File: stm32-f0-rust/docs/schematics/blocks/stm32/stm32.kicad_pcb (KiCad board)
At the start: 2 copper layers, 3 parts, among them J1 Conn_01x05_Female, J2 Conn_01x02_Female, U1 STM32F042F4Px

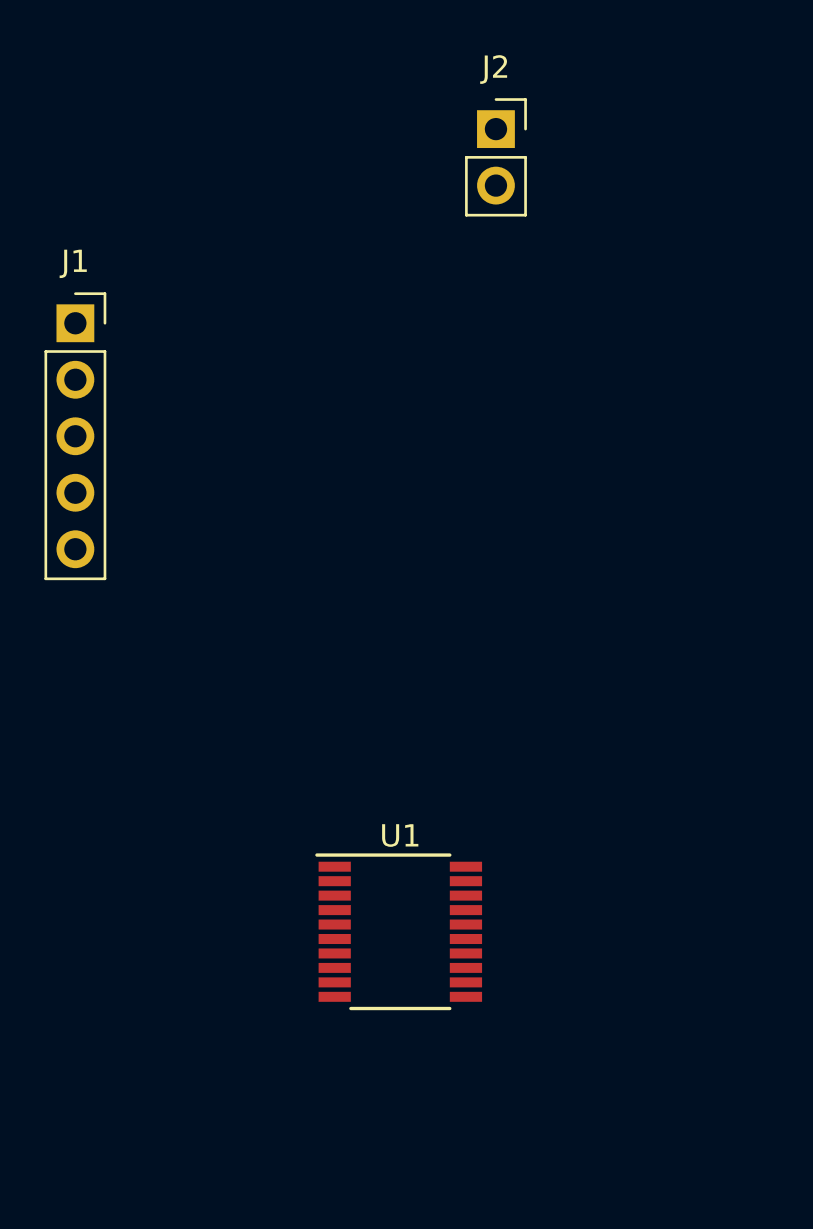
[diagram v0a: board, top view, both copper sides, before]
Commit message: [PCB][STM32-Block] Use single 7-pin socket instead of two.
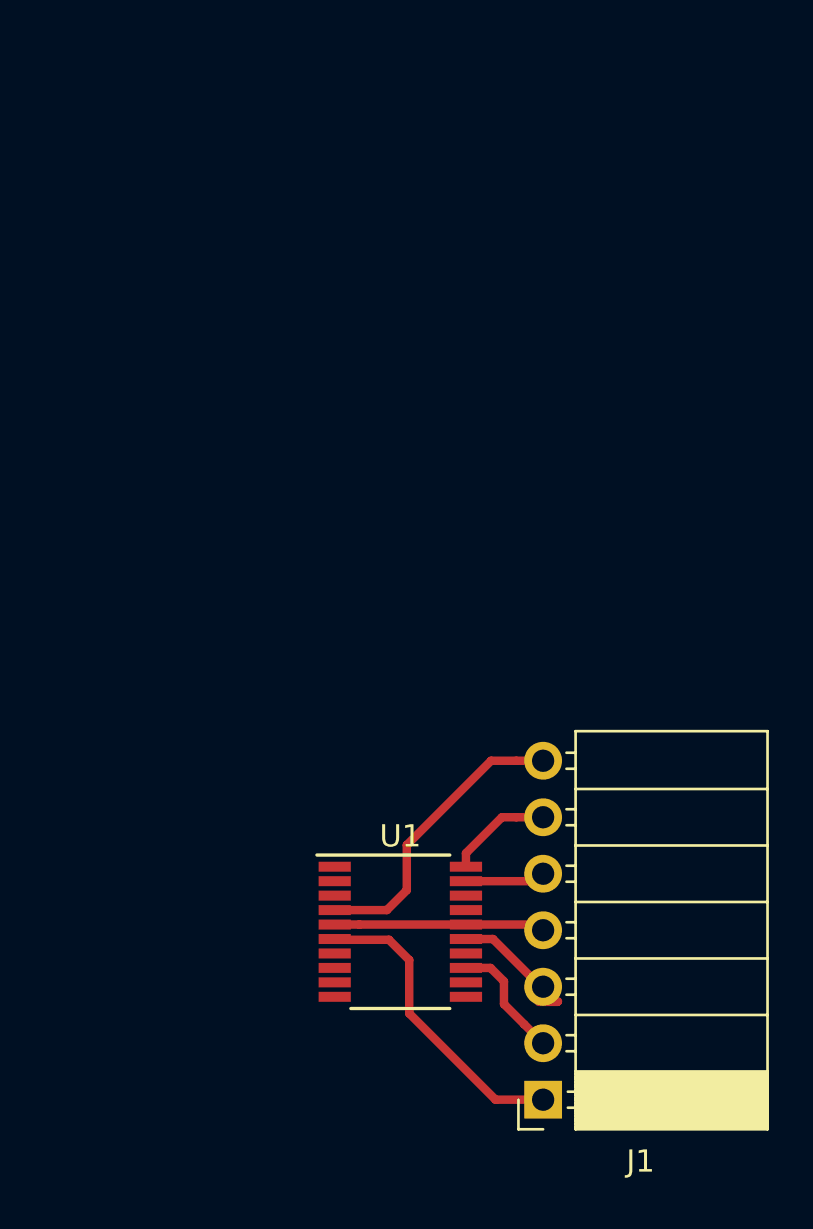
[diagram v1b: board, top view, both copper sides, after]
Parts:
- removed J2: Conn_01x02_Female, Connector_PinSocket_2.54mm:PinSocket_1x02_P2.54mm_Vertical
- J1: value Conn_01x05_Female -> Conn_01x07_Female; footprint Connector_PinSocket_2.54mm:PinSocket_1x05_P2.54mm_Vertical -> Connector_PinSocket_2.54mm:PinSocket_1x07_P2.54mm_Horizontal
- moved J1 40.8 mm to (164.4, 104.7), turned to 180 degrees
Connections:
- J1 pad 1: VDD -> Button
- J1 pad 2: SWCLK -> Buzzer
- J1 pad 4: SWDIO -> VDD
- J1 pad 5: NRST -> SWDIO
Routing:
- net Button: track 0.00 -> 13.8 mm
- net NRST: track 0.00 -> 13.3 mm
- net VDD: track 0.00 -> 9.48 mm
- net Buzzer: track 0.00 -> 5.47 mm
- net GND: track 0.00 -> 5.33 mm
- net SWCLK: track 0.00 -> 5.25 mm
- net SWDIO: track 0.00 -> 3.61 mm

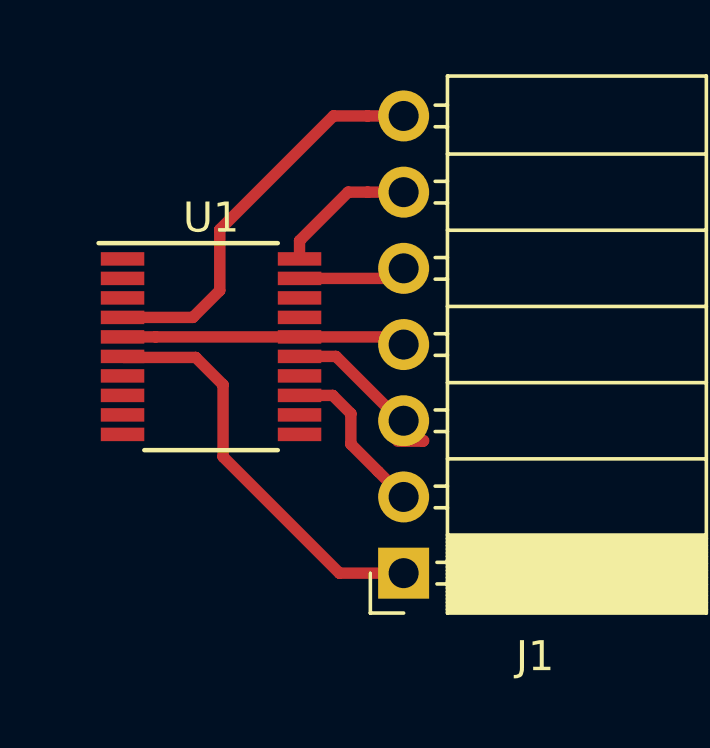
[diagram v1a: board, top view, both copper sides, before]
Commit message: [PCB][STM32-Block] Reduce PCB edges.
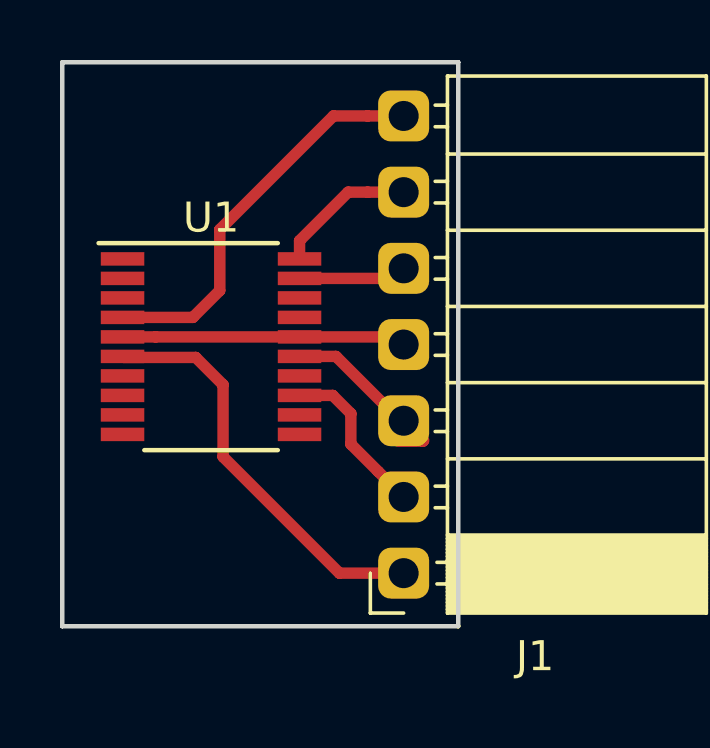
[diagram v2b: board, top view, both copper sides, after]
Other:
- board outline added: 13.2 x 18.8 mm
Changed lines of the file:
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@@
   (general
     (thickness 1.6)
-    (drawings 0)
+    (drawings 4)
     (tracks 35)
     (zones 0)
@@
     (mod_text_size 1 1)
     (mod_text_width 0.15)
-    (pad_size 1.524 1.524)
-    (pad_drill 0.762)
+    (pad_size 1.7 1.7)
+    (pad_drill 1)
     (pad_to_mask_clearance 0.2)
     (aux_axis_origin 0 0)
@@
       (effects (font (size 1 1) (thickness 0.15)))
     )
-    (pad 1 thru_hole rect (at 0 0 180) (size 1.7 1.7) (drill 1) (layers *.Cu *.Mask)
+    (pad 1 thru_hole roundrect (at 0 0 180) (size 1.7 1.7) (drill 1) (layers *.Cu *.Mask)(roundrect_rratio 0.25)
       (net 6 Button))
-    (pad 2 thru_hole oval (at 0 2.54 180) (size 1.7 1.7) (drill 1) (layers *.Cu *.Mask)
+    (pad 2 thru_hole roundrect (at 0 2.54 180) (size 1.7 1.7) (drill 1) (layers *.Cu *.Mask)(roundrect_rratio 0.25)
       (net 13 Buzzer))
-    (pad 3 thru_hole oval (at 0 5.08 180) (size 1.7 1.7) (drill 1) (layers *.Cu *.Mask)
+    (pad 3 thru_hole roundrect (at 0 5.08 180) (size 1.7 1.7) (drill 1) (layers *.Cu *.Mask)(roundrect_rratio 0.25)
       (net 15 GND))
-    (pad 4 thru_hole oval (at 0 7.62 180) (size 1.7 1.7) (drill 1) (layers *.Cu *.Mask)
+    (pad 4 thru_hole roundrect (at 0 7.62 180) (size 1.7 1.7) (drill 1) (layers *.Cu *.Mask)(roundrect_rratio 0.25)
       (net 5 VDD))
-    (pad 5 thru_hole oval (at 0 10.16 180) (size 1.7 1.7) (drill 1) (layers *.Cu *.Mask)
+    (pad 5 thru_hole roundrect (at 0 10.16 180) (size 1.7 1.7) (drill 1) (layers *.Cu *.Mask)(roundrect_rratio 0.25)
       (net 18 SWDIO))
-    (pad 6 thru_hole oval (at 0 12.7 180) (size 1.7 1.7) (drill 1) (layers *.Cu *.Mask)
+    (pad 6 thru_hole roundrect (at 0 12.7 180) (size 1.7 1.7) (drill 1) (layers *.Cu *.Mask)(roundrect_rratio 0.25)
       (net 19 SWCLK))
-    (pad 7 thru_hole oval (at 0 15.24 180) (size 1.7 1.7) (drill 1) (layers *.Cu *.Mask)
+    (pad 7 thru_hole roundrect (at 0 15.24 180) (size 1.7 1.7) (drill 1) (layers *.Cu *.Mask)(roundrect_rratio 0.25)
       (net 4 NRST))
     (model ${KISYS3DMOD}/Connector_PinSocket_2.54mm.3dshapes/PinSocket_1x07_P2.54mm_Horizontal.wrl
@@
     )
   )
+  (gr_line (start 166.2 106.5) (end 166.2 87.7) (layer Edge.Cuts) (width 0.15))
+  (gr_line (start 153 106.5) (end 166.2 106.5) (layer Edge.Cuts) (width 0.15))
+  (gr_line (start 153 87.7) (end 153 106.5) (layer Edge.Cuts) (width 0.15))
+  (gr_line (start 166.2 87.7) (end 153 87.7) (layer Edge.Cuts) (width 0.15))
   (segment (start 163.177919 89.49) (end 164.38 89.49) (width 0.381) (layer F.Cu) (net 4))
   (segment (start 158.25 93.28) (end 162.04 89.49) (width 0.381) (layer F.Cu) (net 4))
